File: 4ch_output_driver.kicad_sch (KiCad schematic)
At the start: 9 parts, among them U6 LTV-247

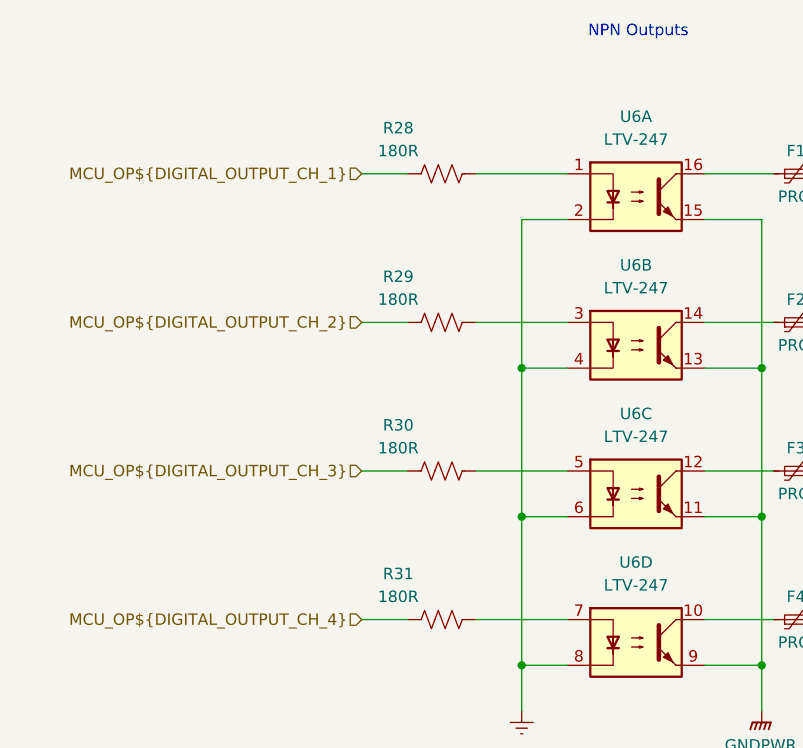
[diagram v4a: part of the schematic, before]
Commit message: Some file changes and output new gerbers + BOM and centroid file for PCBWay Order
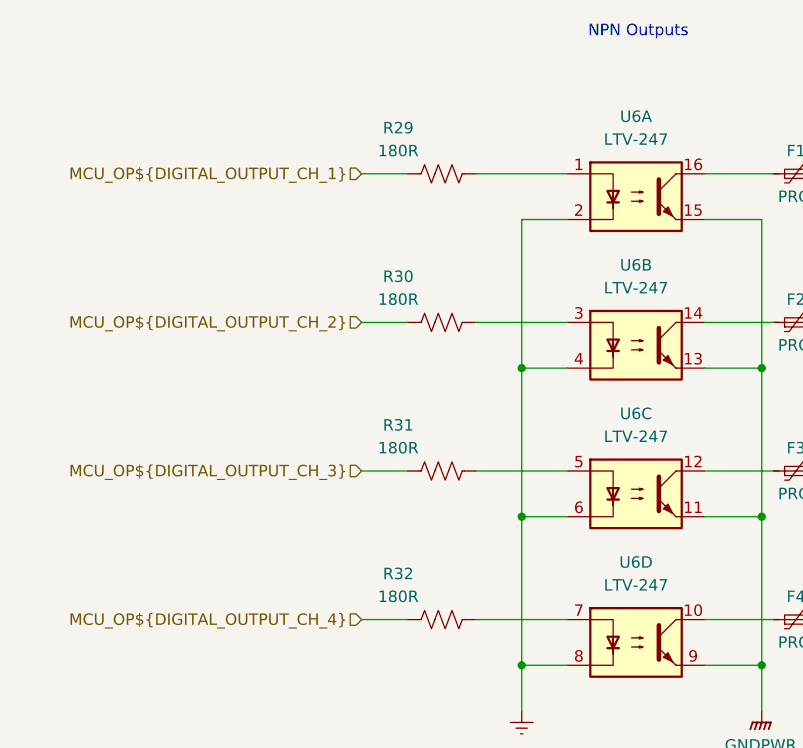
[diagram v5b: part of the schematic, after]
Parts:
- renumbered R28 to R29, R29 to R30, R30 to R31, R31 to R32
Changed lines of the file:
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@@
 		(on_board yes)
 		(dnp no)
-		(property "Reference" "R30"
+		(property "Reference" "R31"
 			(at 118.364 96.52 90)
 			(effects
@@
 			(project "Remora Nucleo F446ZE Hat"
 				(path "/5473abc6-7b93-43cc-a401-f691c4d7d7cf/a10f9653-3098-46b3-8571-958500eea49a/389ca262-c58e-40b0-996c-af5bca34fee3"
-					(reference "R38")
-					(unit 1)
-				)
-				(path "/5473abc6-7b93-43cc-a401-f691c4d7d7cf/a10f9653-3098-46b3-8571-958500eea49a/75bfee9f-dba1-4332-b42b-f74c9030c21f"
-					(reference "R30")
+					(reference "R39")
+					(unit 1)
+				)
+				(path "/5473abc6-7b93-43cc-a401-f691c4d7d7cf/a10f9653-3098-46b3-8571-958500eea49a/75bfee9f-dba1-4332-b42b-f74c9030c21f"
+					(reference "R31")
 					(unit 1)
 				)
@@
 		(on_board yes)
 		(dnp no)
-		(property "Reference" "R28"
+		(property "Reference" "R29"
 			(at 118.364 63.5 90)
 			(effects
@@
 			(project "Remora Nucleo F446ZE Hat"
 				(path "/5473abc6-7b93-43cc-a401-f691c4d7d7cf/a10f9653-3098-46b3-8571-958500eea49a/389ca262-c58e-40b0-996c-af5bca34fee3"
-					(reference "R36")
-					(unit 1)
-				)
-				(path "/5473abc6-7b93-43cc-a401-f691c4d7d7cf/a10f9653-3098-46b3-8571-958500eea49a/75bfee9f-dba1-4332-b42b-f74c9030c21f"
-					(reference "R28")
+					(reference "R37")
+					(unit 1)
+				)
+				(path "/5473abc6-7b93-43cc-a401-f691c4d7d7cf/a10f9653-3098-46b3-8571-958500eea49a/75bfee9f-dba1-4332-b42b-f74c9030c21f"
+					(reference "R29")
 					(unit 1)
 				)
@@
 		(on_board yes)
 		(dnp no)
-		(property "Reference" "R29"
+		(property "Reference" "R30"
 			(at 118.364 80.01 90)
 			(effects
@@
 			(project "Remora Nucleo F446ZE Hat"
 				(path "/5473abc6-7b93-43cc-a401-f691c4d7d7cf/a10f9653-3098-46b3-8571-958500eea49a/389ca262-c58e-40b0-996c-af5bca34fee3"
-					(reference "R37")
-					(unit 1)
-				)
-				(path "/5473abc6-7b93-43cc-a401-f691c4d7d7cf/a10f9653-3098-46b3-8571-958500eea49a/75bfee9f-dba1-4332-b42b-f74c9030c21f"
-					(reference "R29")
+					(reference "R38")
+					(unit 1)
+				)
+				(path "/5473abc6-7b93-43cc-a401-f691c4d7d7cf/a10f9653-3098-46b3-8571-958500eea49a/75bfee9f-dba1-4332-b42b-f74c9030c21f"
+					(reference "R30")
 					(unit 1)
 				)
@@
 		(on_board yes)
 		(dnp no)
-		(property "Reference" "R31"
+		(property "Reference" "R32"
 			(at 118.364 113.03 90)
 			(effects
@@
 			(project "Remora Nucleo F446ZE Hat"
 				(path "/5473abc6-7b93-43cc-a401-f691c4d7d7cf/a10f9653-3098-46b3-8571-958500eea49a/389ca262-c58e-40b0-996c-af5bca34fee3"
-					(reference "R39")
-					(unit 1)
-				)
-				(path "/5473abc6-7b93-43cc-a401-f691c4d7d7cf/a10f9653-3098-46b3-8571-958500eea49a/75bfee9f-dba1-4332-b42b-f74c9030c21f"
-					(reference "R31")
-					(unit 1)
-				)
+					(reference "R40")
+					(unit 1)
+				)
+				(path "/5473abc6-7b93-43cc-a401-f691c4d7d7cf/a10f9653-3098-46b3-8571-958500eea49a/75bfee9f-dba1-4332-b42b-f74c9030c21f"
+					(reference "R32")
+					(unit 1)
+				)
